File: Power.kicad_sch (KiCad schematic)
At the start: 4 parts, among them J2 A/C, U1 L7805 module, U2 L7812 module

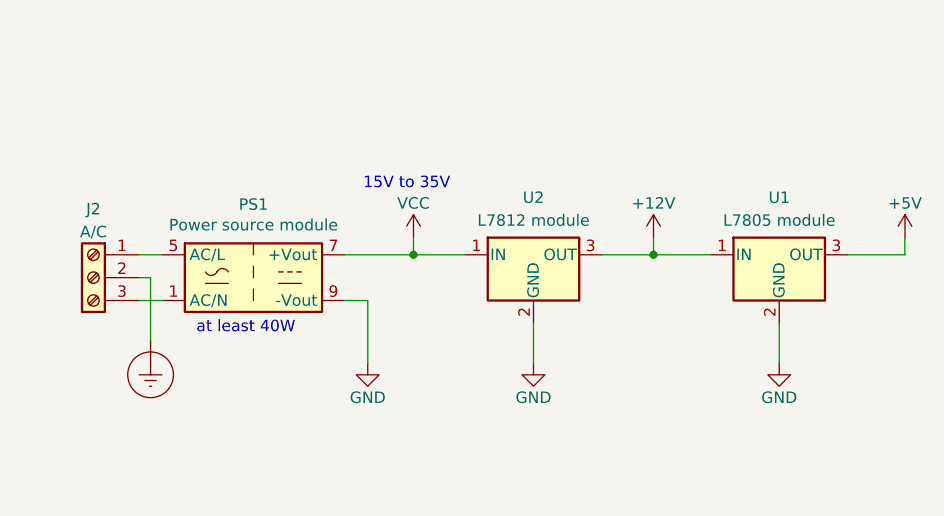
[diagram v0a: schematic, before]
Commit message: Using two LM317s instead of a LM7812 + LM7805
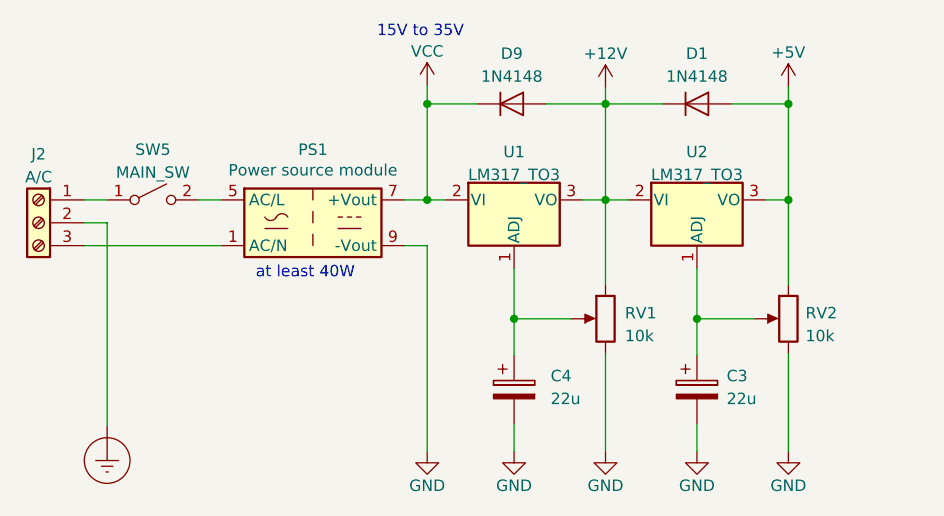
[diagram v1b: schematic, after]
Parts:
- removed U1: L7805 module, symbol Regulator_Linear:L7805
- removed U2: L7812 module, symbol Regulator_Linear:L7812
- added C3, C4: 22u, symbol device:CP
- added D1, D9: 1N4148, Diodes_THT:D_DO-35_SOD27_Horizontal_RM10, symbol diode:1N4148
- added RV1, RV2: 10k, symbol device:POT
- added SW5: MAIN_SW, symbol switches:SW_SPST
- added U1, U2: LM317_TO3, TO_SOT_Packages_THT:TO-3, symbol regul:LM317_TO3
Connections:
- net +12V: now also D1.1 (K), D9.2 (A), RV1.1, U1.3 (VO), U2.2 (VI)
- net +5V: now also D1.2 (A), RV2.1, U2.3 (VO)
- net GND: now also C3.2, C4.2, RV1.3, RV2.3
- net VCC: now also D9.1 (K), U1.2 (VI)
- net at J2.1 (Pin_1): now also SW5.1 (A); no longer PS1.5 (AC/L)
- new net: C4.1, RV1.2, U1.1 (ADJ)
- new net: C3.1, RV2.2, U2.1 (ADJ)
- new net: PS1.5 (AC/L), SW5.2 (B)
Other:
- moved on the sheet: J2, PS1

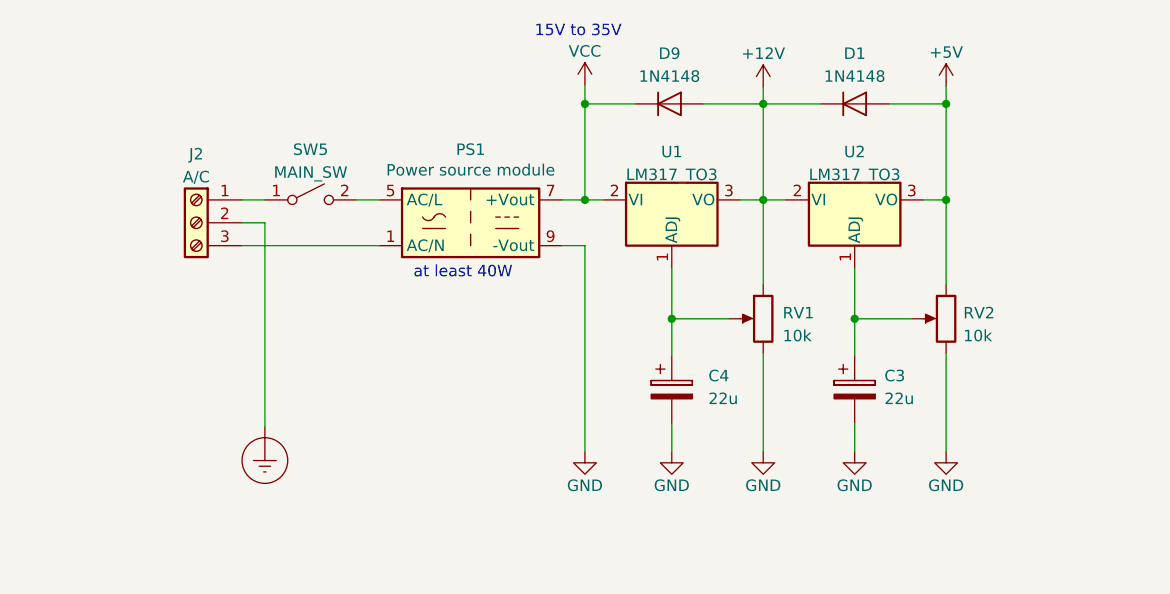
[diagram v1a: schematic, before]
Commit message: Using two LM317s instead of a LM7812 + LM7805 and KiCAD 8.0.3rc1
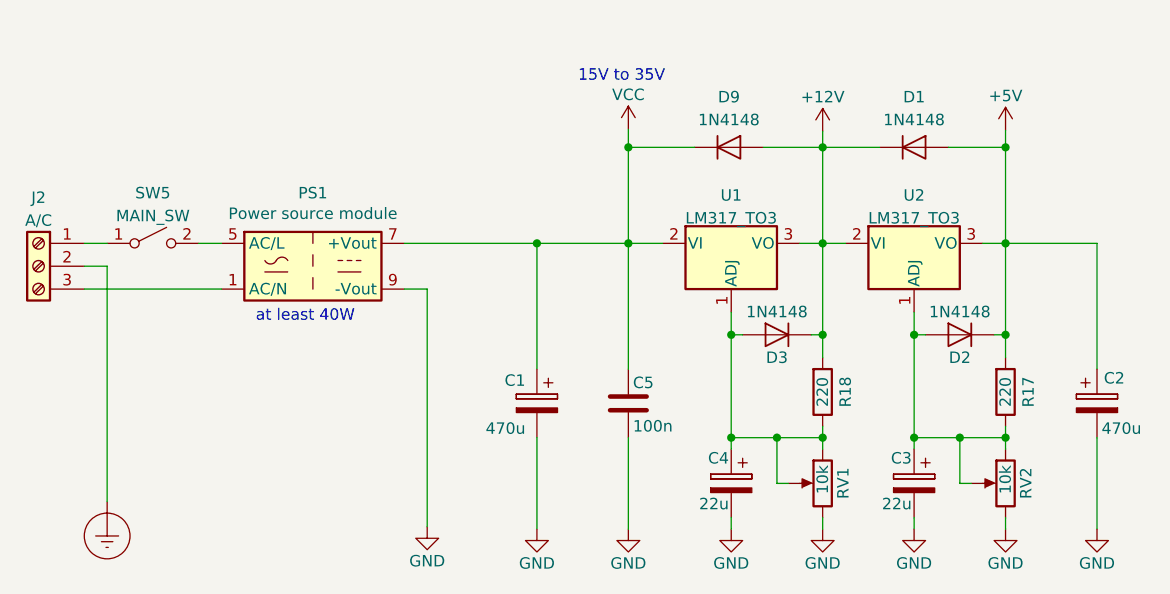
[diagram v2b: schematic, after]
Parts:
- added C1, C2: 470u, symbol device:CP
- added C5: 100n, symbol Device:C
- added D2, D3: 1N4148, Diodes_THT:D_DO-35_SOD27_Horizontal_RM10, symbol diode:1N4148
- added R17, R18: 220, symbol Device:R
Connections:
- net +12V: now also D3.1 (K), R18.2; no longer RV1.1
- net +5V: now also C2.1, D2.1 (K), R17.2; no longer RV2.1
- net GND: now also C1.2, C2.2, C5.2
- net VCC: now also C1.1, C5.1
- net at C4.1, RV1.2, U1.1 (ADJ): now also RV1.1, D3.2 (A), R18.1
- net at C3.1, RV2.2, U2.1 (ADJ): now also RV2.1, D2.2 (A), R17.1
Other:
- moved on the sheet: C4, D1, D9, J2, PS1, RV1, SW5, U1, U2

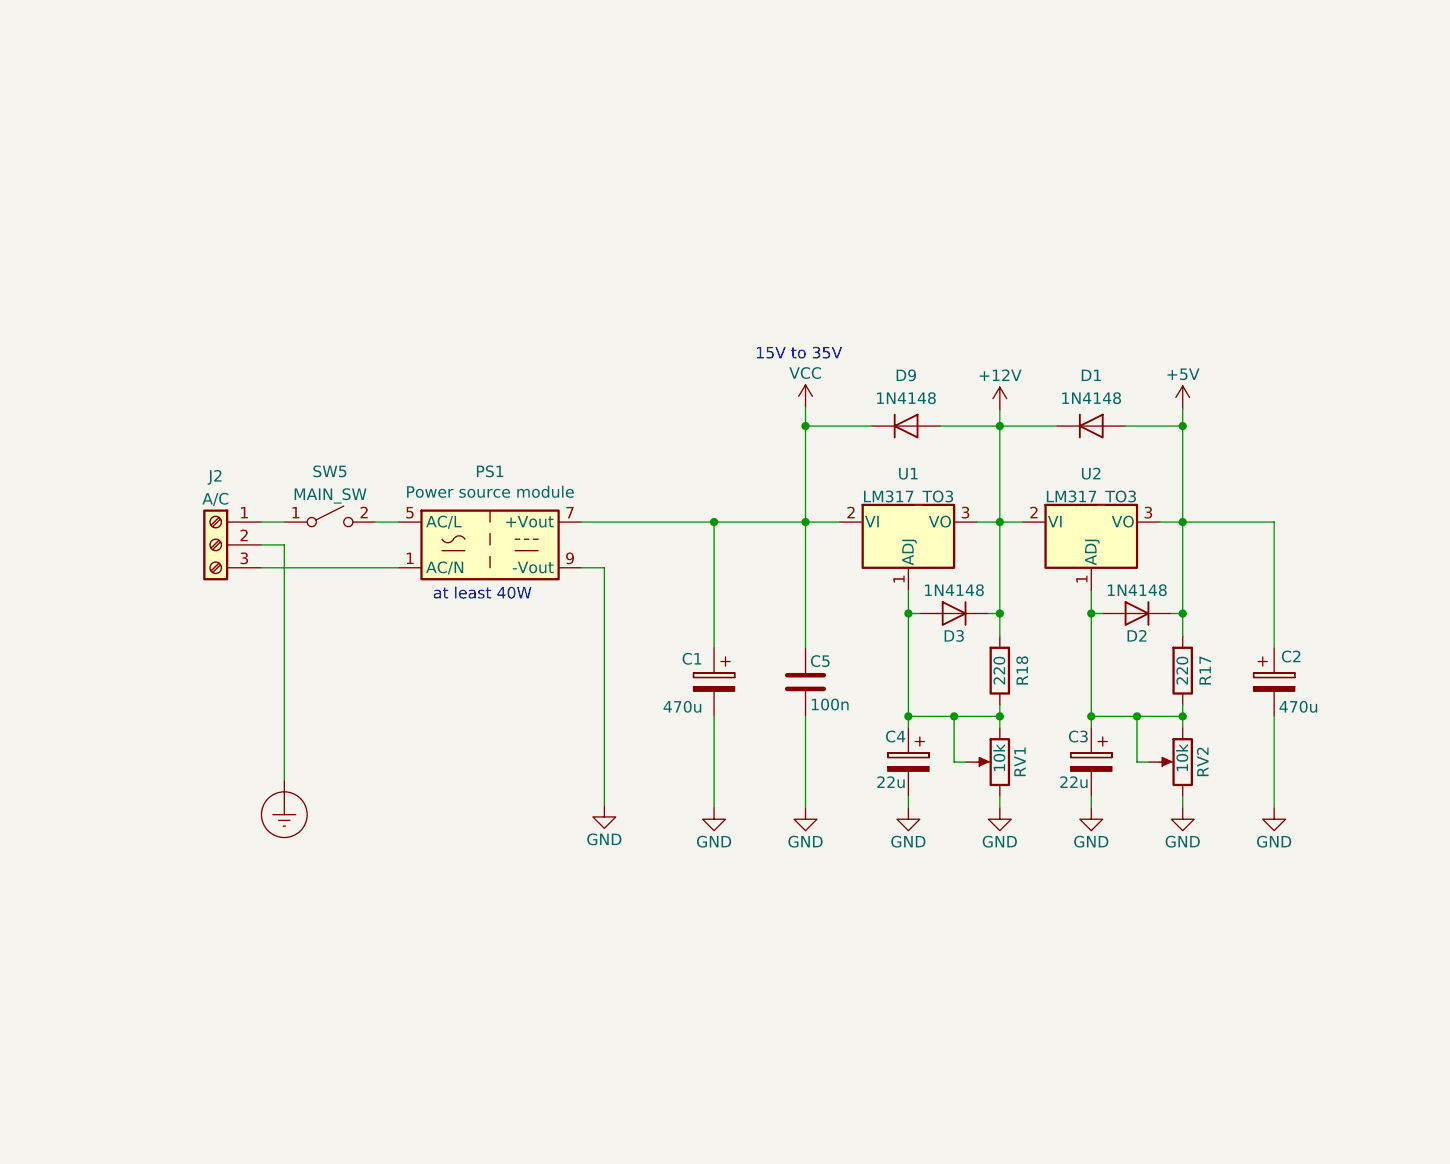
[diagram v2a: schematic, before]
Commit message: - Power rack alternatives: either two LM317s or LM7812 + LM7805 - Added channels SPDT selectors for foot switch or external output enable control
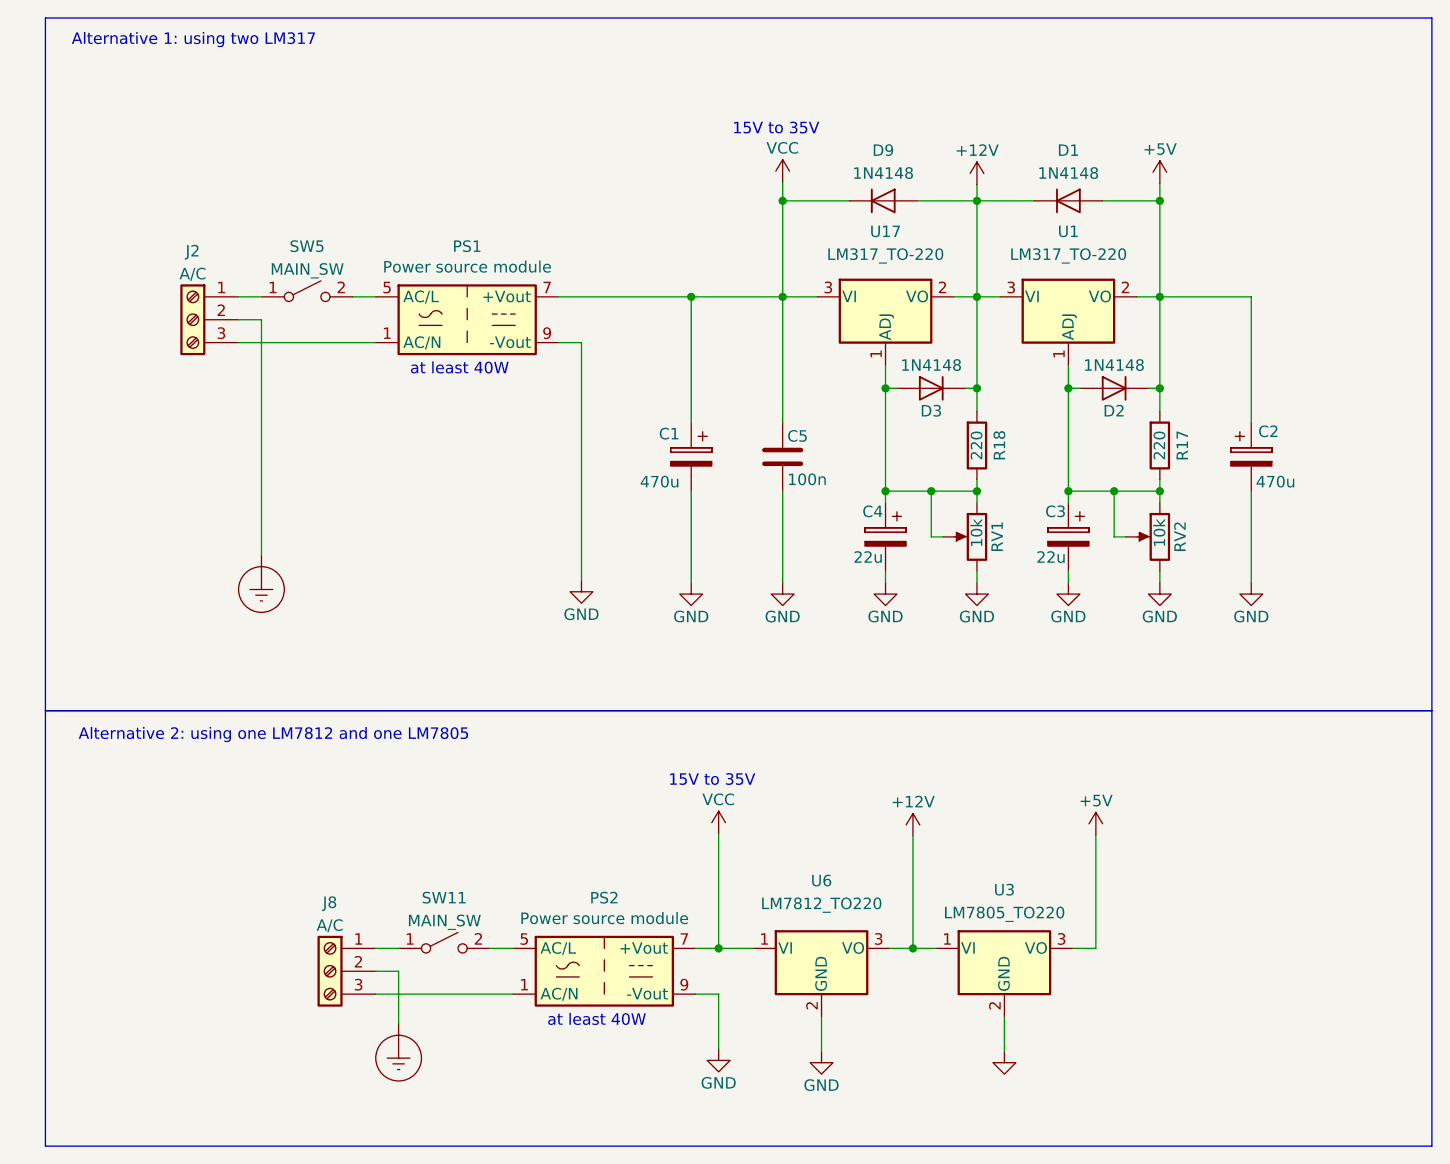
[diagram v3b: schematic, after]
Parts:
- removed U1, U2: LM317_TO3, TO_SOT_Packages_THT:TO-3, symbol regul:LM317_TO3
- added J8: A/C, symbol Connector:Screw_Terminal_01x03
- added PS2: Power source module, Converter_ACDC:Converter_ACDC_Hahn_HS-400xx_THT, symbol Converter_ACDC:HS-40024
- added SW11: MAIN_SW, symbol switches:SW_SPST
- added U1, U17: LM317_TO-220, Package_TO_SOT_THT:TO-220-3_Vertical, symbol Regulator_Linear:LM317_TO-220
- added U3: LM7805_TO220, Package_TO_SOT_THT:TO-220-3_Vertical, symbol Regulator_Linear:LM7805_TO220
- added U6: LM7812_TO220, Package_TO_SOT_THT:TO-220-3_Vertical, symbol Regulator_Linear:LM7812_TO220
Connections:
- net +12V: now also U1.3 (VI), U17.2 (VO), U3.1 (VI), U6.3 (VO)
- net +5V: now also U1.2 (VO), U3.3 (VO)
- net Earth_Protective: now also J8.2 (Pin_2)
- net GND: now also PS2.9 (-Vout), U3.2 (GND), U6.2 (GND)
- net VCC: now also PS2.7 (+Vout), U17.3 (VI), U6.1 (VI)
- net at C4.1, D3.2 (A), R18.1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: now also U17.1 (ADJ)
- net at C3.1, D2.2 (A), R17.1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: now also U1.1 (ADJ)
- new net: J8.3 (Pin_3), PS2.1 (AC/N)
- new net: PS2.5 (AC/L), SW11.2 (B)
- new net: J8.1 (Pin_1), SW11.1 (A)
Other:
- note added: "Alternative 1: using two LM317"
- note added: "Alternative 2: using one LM7812 and one LM7805"
- moved on the sheet: C1, C2, C3, C4, C5, D1, D2, D3, D9, J2, PS1, R17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

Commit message: Adding capacitors to stabilize voltages, changed the LED driver connector
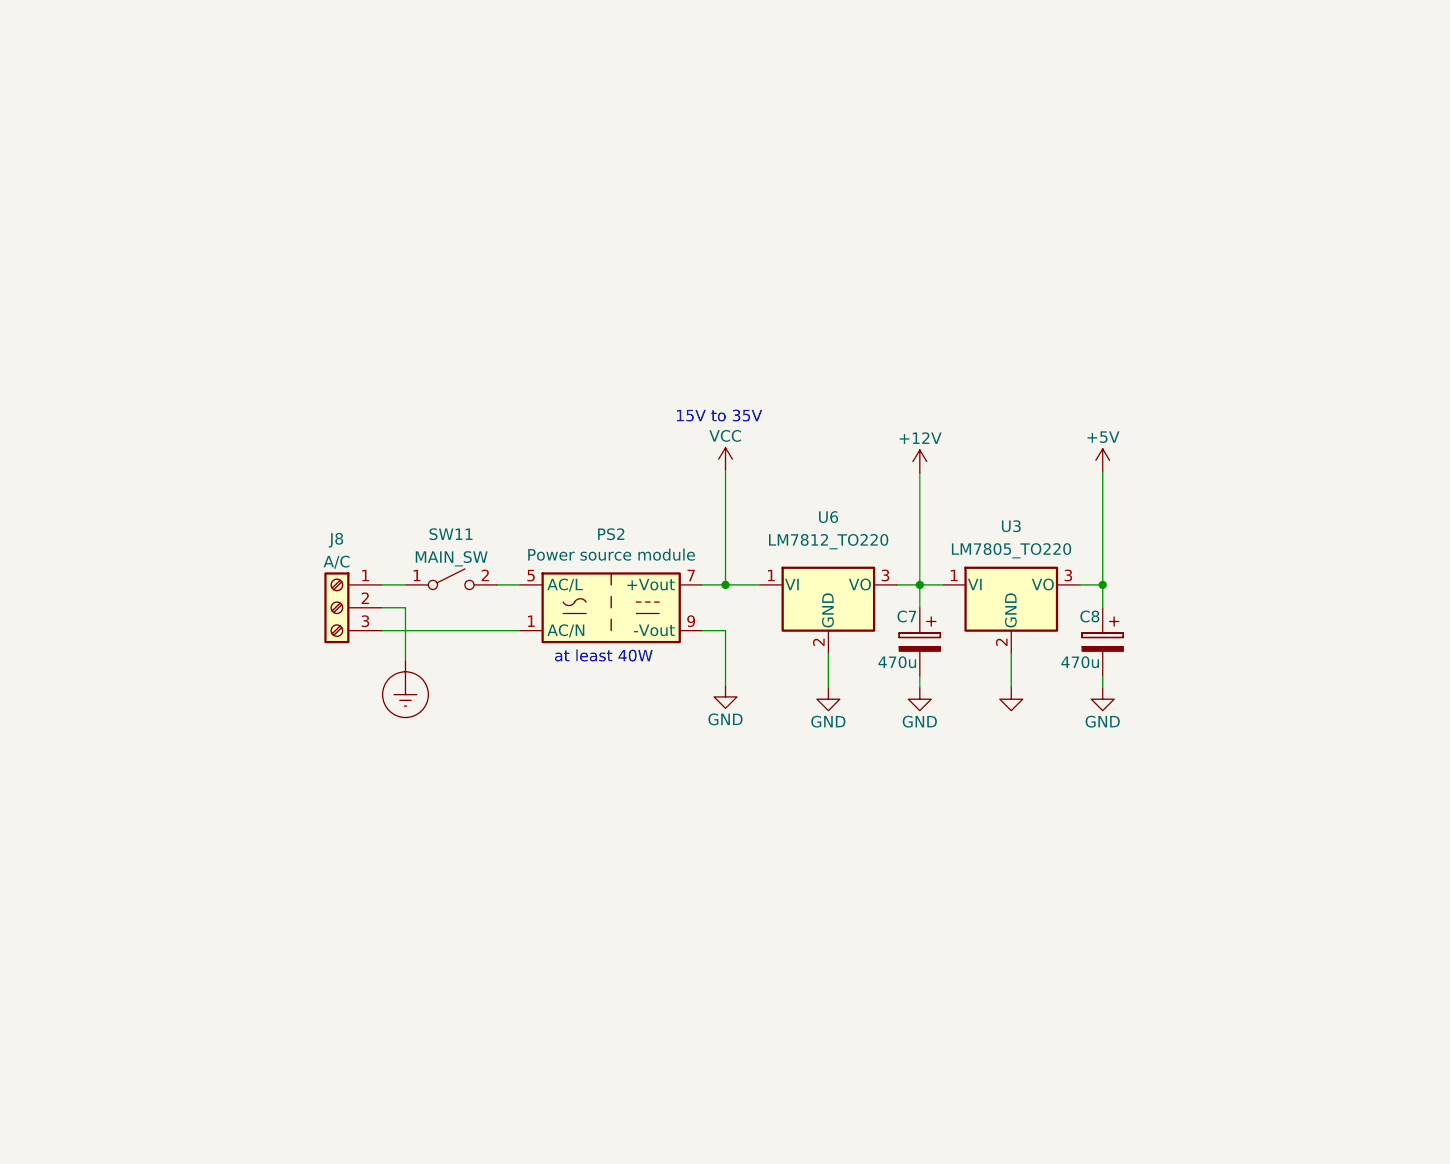
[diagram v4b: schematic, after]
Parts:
- removed C1, C2: 470u, symbol device:CP
- removed C3, C4: 22u, symbol device:CP
- removed C5: 100n, symbol Device:C
- removed D1, D2, D3, D9: 1N4148, Diodes_THT:D_DO-35_SOD27_Horizontal_RM10, symbol diode:1N4148
- removed J2: A/C, symbol Connector:Screw_Terminal_01x03
- removed PS1: Power source module, Converter_ACDC:Converter_ACDC_Hahn_HS-400xx_THT, symbol Converter_ACDC:HS-40024
- removed R17, R18: 220, symbol Device:R
- removed RV1, RV2: 10k, symbol device:POT
- removed SW5: MAIN_SW, symbol switches:SW_SPST
- removed U1, U17: LM317_TO-220, Package_TO_SOT_THT:TO-220-3_Vertical, symbol Regulator_Linear:LM317_TO-220
- added C7, C8: 470u, symbol device:CP
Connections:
- net +12V: now also C7.1
- net +5V: now also C8.1
- net GND: now also C7.2, C8.2
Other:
- note removed: "Alternative 1: using two LM317"
- note removed: "Alternative 2: using one LM7812 and one LM7805"
- moved on the sheet: J8, PS2, SW11, U3, U6
